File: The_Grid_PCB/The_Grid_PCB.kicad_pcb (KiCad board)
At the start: 2 copper layers, 120 x 75 mm, 104 parts, among them J1 TC2050, J10 Screw_Terminal_01x02, J11 Screw_Terminal_01x02, J12 Screw_Terminal_01x02, J13 Screw_Terminal_01x02, J14 Screw_Terminal_01x02, J15 Screw_Terminal_01x02, J16 Screw_Terminal_01x02, J17 Screw_Terminal_01x02, J2 Screw_Terminal_01x02, J3 Conn_01x02, J4 Conn_01x02, J5 Screw_Terminal_01x02, J6 Screw_Terminal_01x02, J7 Screw_Terminal_01x02, J8 Screw_Terminal_01x02, J9 Screw_Terminal_01x02, Q1 AO3400A, Q10 AO3400A, Q11 AO3400A, Q12 AO3400A, Q2 AO3400A, Q3 AO3400A, Q4 AO3400A, Q5 AO3400A, Q6 AO3400A, Q7 AO3400A, Q8 AO3400A, Q9 AO3400A, U1 STM32F030C8Tx, U2 SN65HVD11HD, U3 TPS54331DR, X1 X322516MLB4SI

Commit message: update wiring diagram again sob
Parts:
- removed the R11 at (147.0, 90.9)
- removed the R14 at (141.3, 90.1)
- removed the R8 at (179.0, 106.1)
- added C21: 47uF, PCM_JLCPCB:C_1206, F.Cu at (256.9, 87.5)
- added C22: 22uF, PCM_JLCPCB:C_0603, F.Cu at (256.0, 95.9)
- added C24: 100nF, PCM_JLCPCB:C_0805, F.Cu at (242.7, 95.5)
- added D2: LED, PCM_JLCPCB:D_0603, F.Cu at (247.0, 95.3)
- added R12: 68kΩ, PCM_JLCPCB:R_0603, F.Cu at (134.4, 92.5)
- added R16: 560Ω, PCM_JLCPCB:R_0603, F.Cu at (128.8, 93.3)
- added R17: 1.2kΩ, PCM_JLCPCB:R_0603, F.Cu at (127.0, 95.0)
- added R2: 1.5kΩ, PCM_JLCPCB:R_0603, F.Cu at (252.3, 86.9)
- added R7: 10Ω, PCM_JLCPCB:R_0603, F.Cu at (252.3, 91.4)
- added R9: 120, Resistor_THT:R_Axial_DIN0207_L6.3mm_D2.5mm_P10.16mm_Horizontal, F.Cu at (242.9, 122.0)
- added U4: AMS1117-3.3, Package_TO_SOT_SMD:SOT-223-3_TabPin2, F.Cu at (227.5, 80.8)
- C19: value 100uF -> 10uF; footprint PCM_JLCPCB:C_1206 -> PCM_JLCPCB:C_0603
- C20: value 100uF -> 47uF
- J1: footprint Connector:Tag-Connect_TC2070-IDC-FP_2x07_P1.27mm_Vertical -> Connector:Tag-Connect_TC2050-IDC-FP_2x05_P1.27mm_Vertical
- L1: value 6.8uH -> 8.2uH; footprint Inductor_SMD:L_Sumida_CDMC6D28_7.25x6.5mm -> Inductor_SMD:L_Bourns_SRP7028A_7.3x6.6mm
- R15: value 240Ω -> 200Ω
- U2: value SN65HVD11HD -> SN65HVD485EDR
- moved C20 107.8 mm to (256.9, 90.8), turned to 0 degrees
- moved C19 104.1 mm to (256.0, 93.6), turned to 0 degrees
- moved D1 62.2 mm to (222.6, 97.3)
- moved R1 62.2 mm to (222.5, 95.3)
- moved R15 14.4 mm to (127.0, 91.6)
- moved C11 12.6 mm to (157.1, 95.2)
- moved C12 12.6 mm to (163.1, 93.7)
- moved C13 12.6 mm to (154.6, 95.2)
- moved C14 12.6 mm to (149.6, 95.2)
- moved C15 12.6 mm to (149.1, 90.2)
- moved C16 12.6 mm to (140.1, 97.7)
- moved C17 12.6 mm to (131.6, 93.2)
- moved C18 12.6 mm to (137.1, 93.2)
- moved C23 12.6 mm to (134.1, 107.4)
- moved C25 12.6 mm to (134.1, 105.1)
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- renumbered C21 to C23, C22 to C25, D2 to D3, D3 to D4, R9 to R10, R10 to R11, R12 to R13, R13 to R14, R16 to R18, R17 to R19, R18 to R20, R19 to R21, R20 to R22, R21 to R23, R22 to R24, R23 to R25, R24 to R26, R25 to R27, R26 to R28, R27 to R29, R2 to R3, R28 to R30, R29 to R31, R30 to R32, R31 to R33, R32 to R34, R33 to R35, R34 to R36, R35 to R37, R36 to R38, R37 to R39, R3 to R4, R38 to R40, R39 to R41, R40 to R42, R41 to R43, R4 to R5, R5 to R6, R7 to R8
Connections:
- C10 pad 1: +3.3V -> +5V
- C19 pad 1: +3.3V -> +5V
- C20 pad 1: +3.3V -> GND
- C20 pad 2: GND -> +5V
- C23 pad 1: +3.3V -> +5V
- C25 pad 1: +3.3V -> +5V
- L1 pad 2: +3.3V -> +5V
- R13 pad 1: +3.3V -> +5V
- R15 pad 1: Net-(R14-Pad2) -> Net-(U3-VSENSE)
- R15 pad 2: GND -> Net-(R15-Pad2)
- R5 pad 1: +3.3V -> +5V
- U2 pad 8: +3.3V -> +5V
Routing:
- net GND: track 574.4 -> 457.6 mm
- net +3.3V: track 280.9 -> 192.2 mm, vias 7 -> 6
- net /R4: track 55.0 -> 0.00 mm
- net /G4: track 52.8 -> 0.00 mm
- net /B3: track 46.2 -> 0.00 mm
- net /G3: track 44.6 -> 0.00 mm
- net /B4: track 44.1 -> 0.00 mm
- net /R3: track 43.0 -> 0.00 mm
- net +5V: track 0.00 -> 35.9 mm
- net /B1: track 35.7 -> 0.00 mm
- net /B2: track 33.7 -> 0.00 mm
- net /R2: track 31.4 -> 0.00 mm
- net /G2: track 31.2 -> 0.00 mm
- net /R1: track 34.6 -> 7.89 mm
- net /G1: track 33.1 -> 6.86 mm
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- added copper zone on F.Cu, net +5V
- removed copper zone on F.Cu, net +3.3V
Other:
- board size 120 x 75 mm -> 120 x 60 mm

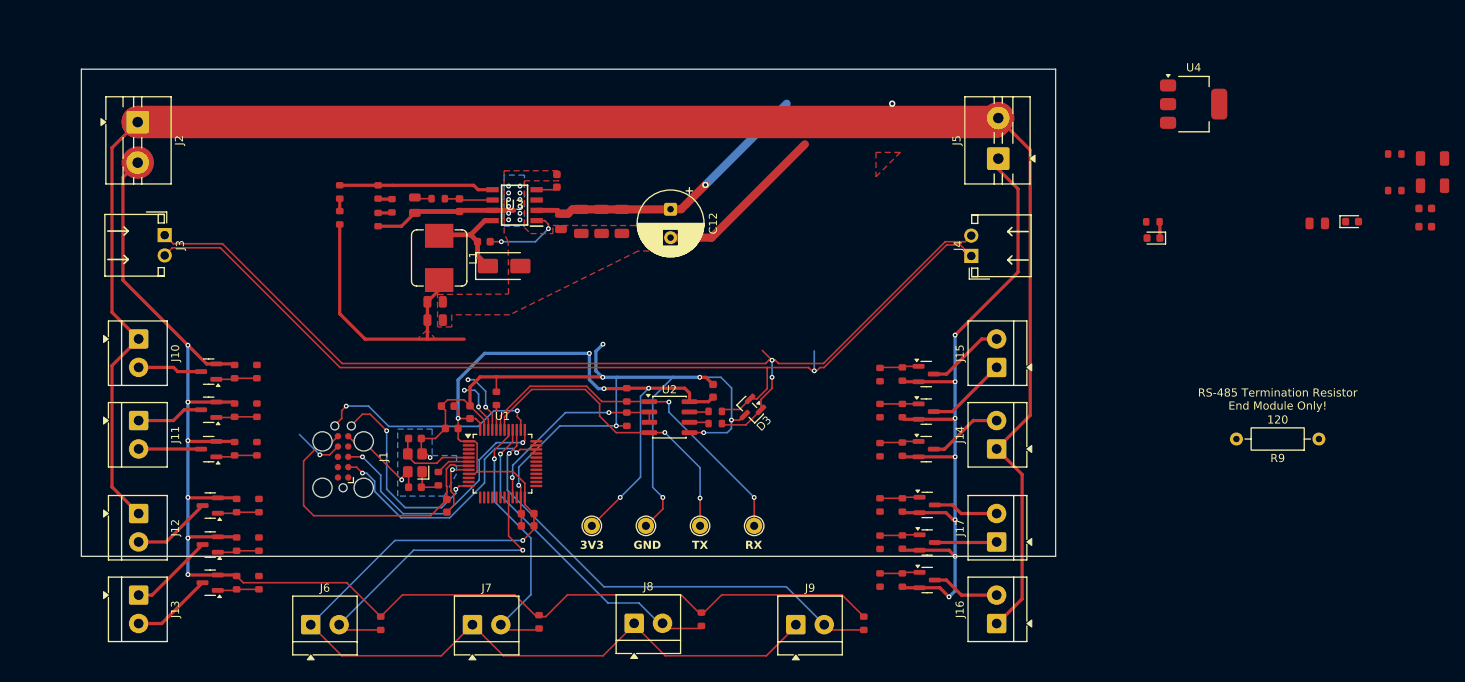
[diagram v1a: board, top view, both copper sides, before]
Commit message: revised pcb nevin/miguel feedback
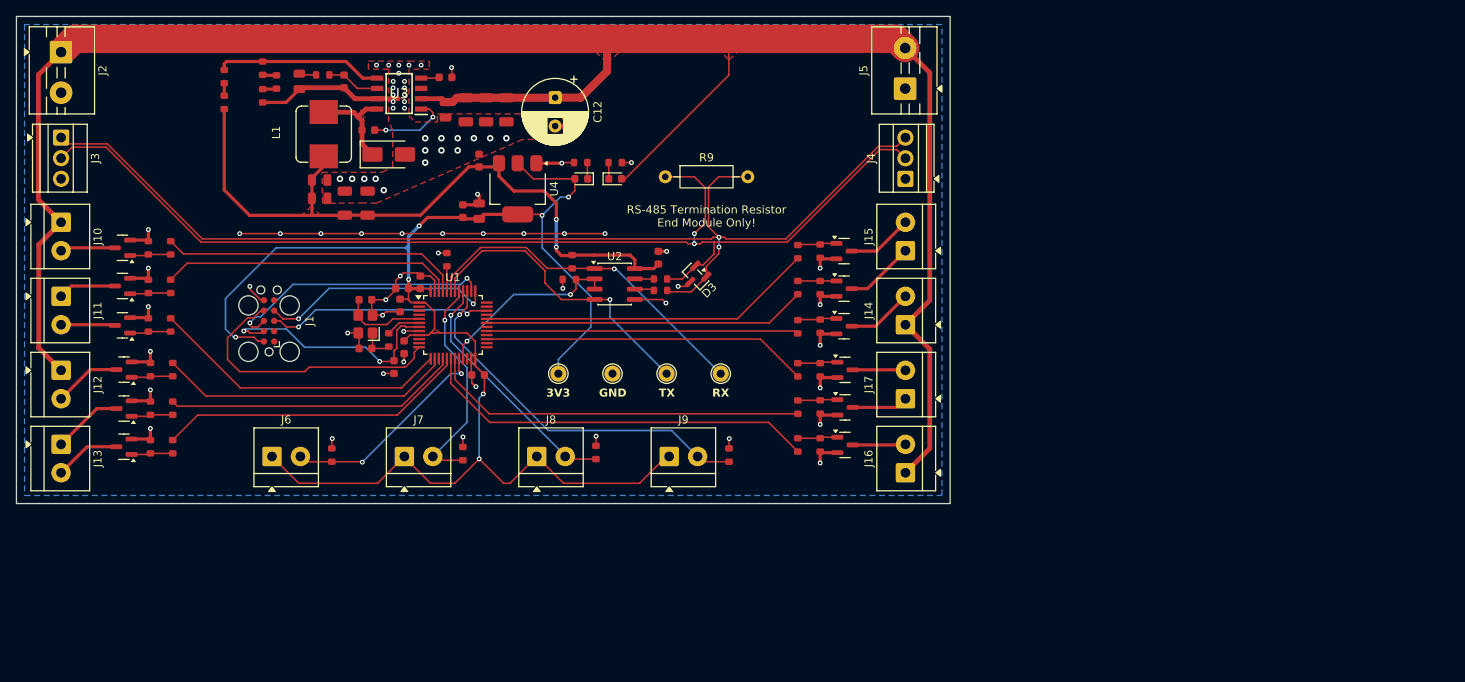
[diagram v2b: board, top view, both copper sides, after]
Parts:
- removed the R6 at (157.7, 119.6)
- removed the R6 at (168.6, 118.6)
- added R6: 10kΩ, PCM_JLCPCB:R_0603, F.Cu at (150.6, 102.4)
- J3, J4: value Conn_01x02 -> Screw_Terminal_01x03; footprint james_custom_footprint_library:JST_XH_B02B-XH-A_02x2.50mm_7.32x7.5_RightAngle -> TerminalBlock:TerminalBlock_Xinya_XY308-2.54-3P_1x03_P2.54mm_Horizontal
- moved C20 134.0 mm to (123.0, 93.0), turned to -90 degrees
- moved C21 131.3 mm to (125.8, 93.0), turned to -90 degrees
- moved C22 118.6 mm to (137.5, 94.0), turned to 90 degrees
- moved C19 116.7 mm to (139.5, 87.8), turned to 90 degrees
- moved C24 103.3 mm to (139.5, 94.0), turned to 90 degrees
- moved R2 96.0 mm to (156.2, 88.0)
- moved R7 91.1 mm to (161.8, 102.3)
- moved D2 90.9 mm to (156.2, 90.0)
- moved R9 86.7 mm to (162.4, 89.8), turned to 0 degrees
- moved U4 83.9 mm to (144.2, 91.2), turned to -90 degrees
- moved D1 70.9 mm to (152.1, 90.0)
- moved R1 70.9 mm to (152.0, 88.0)
- moved C5 32.8 mm to (132.2, 102.8), turned to 90 degrees
- moved R19 26.5 mm to (170.3, 124.0)
- moved J9 25.9 mm to (162.9, 124.2)
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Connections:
- J4 pad 1: /RSB -> GND
- J4 pad 2: /RSA -> /RSB
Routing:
- net GND: track 457.6 -> 162.3 mm, vias 36 -> 75
- net +5V: track 35.9 -> 86.0 mm, vias 0 -> 2
- net /R4: track 0.00 -> 49.3 mm
- net /G4: track 0.00 -> 46.5 mm
- net /B3: track 0.00 -> 41.4 mm
- net /B4: track 0.00 -> 40.2 mm
- net /G3: track 0.00 -> 39.8 mm
- net /R3: track 0.00 -> 38.4 mm
- net /B2: track 0.00 -> 38.4 mm
- net /B1: track 0.00 -> 37.1 mm
- net /G2: track 0.00 -> 36.4 mm
- net /R2: track 0.00 -> 36.3 mm
- net /R1: track 7.89 -> 37.2 mm, vias 2 -> 0
- net /G1: track 6.86 -> 36.1 mm, vias 2 -> 0
- net /Microswitch4: track 58.9 -> 46.4 mm
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- added copper zone on F.Cu, net +24V
- added copper zone on B.Cu, net +3.3V
- added copper zone on F.Cu, net +3.3V
- added copper zone on F.Cu, net Net-(U3-PH)
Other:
- board size 120 x 60 mm -> 115 x 60 mm

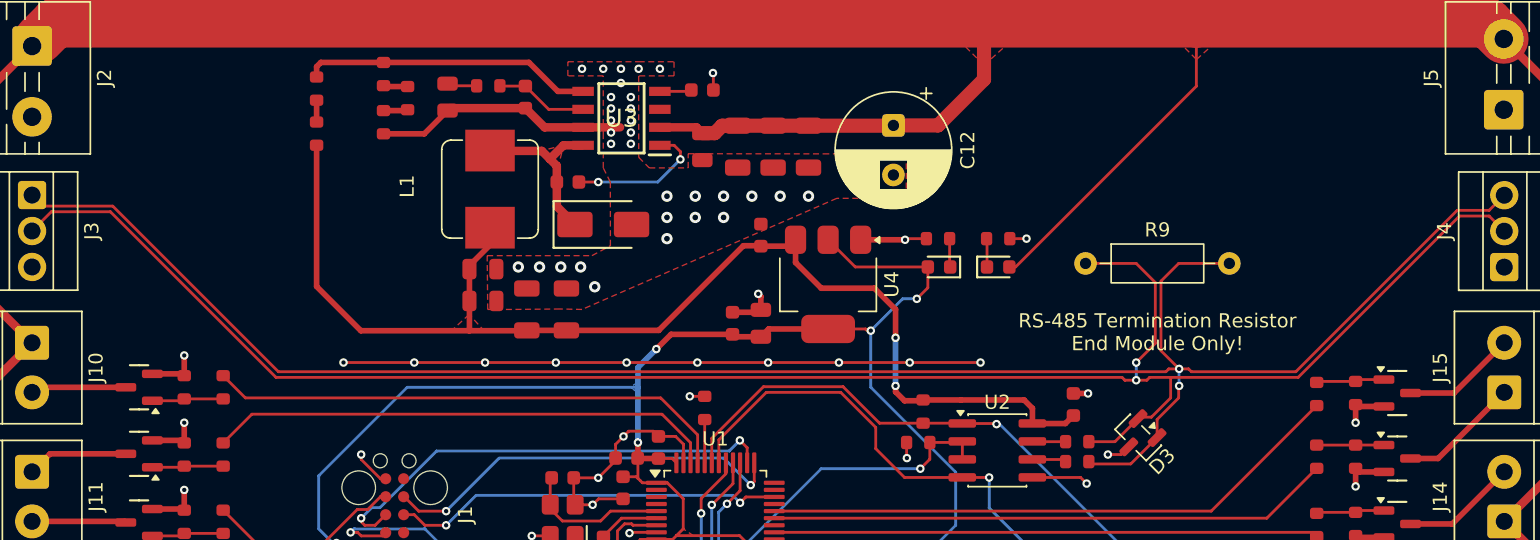
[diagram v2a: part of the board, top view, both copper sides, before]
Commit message: add silkscreen, move termination res
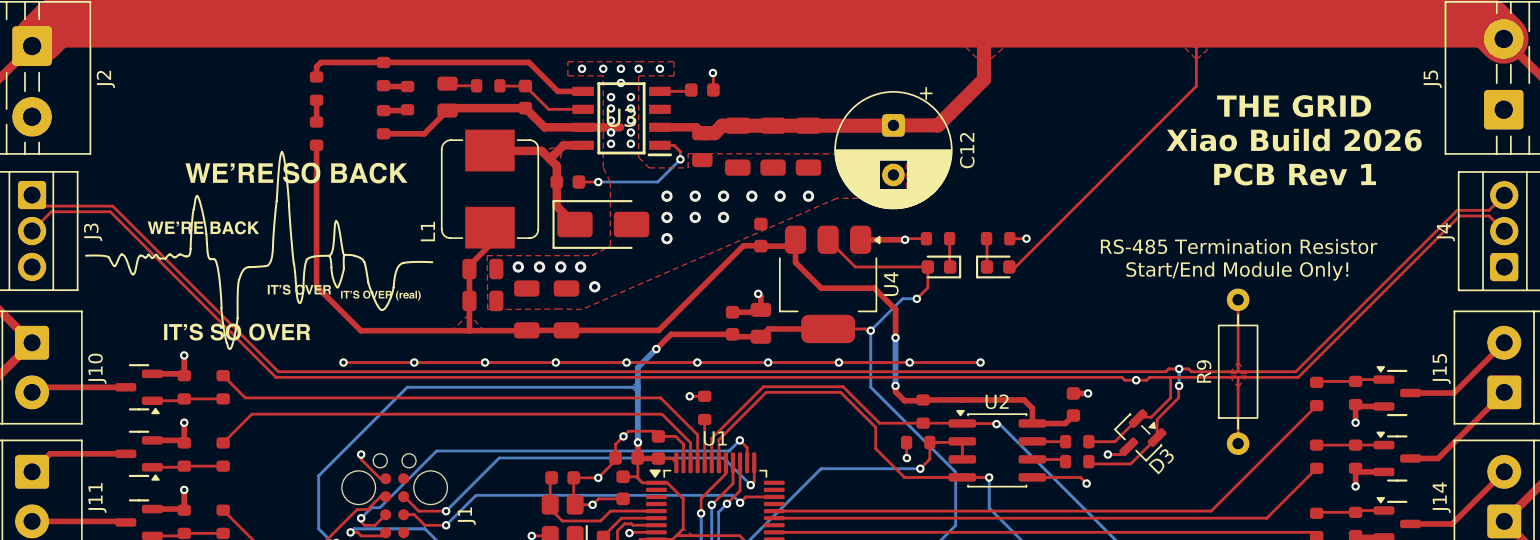
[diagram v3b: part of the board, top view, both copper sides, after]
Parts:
- moved R9 16.7 mm to (173.2, 102.5), turned to 90 degrees
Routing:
- net /RSB: track 136.2 -> 127.9 mm, vias 2 -> 1
- net /RSA: track 137.5 -> 130.5 mm
- added copper zone on F.Cu, net /RSA
- added copper zone on F.Cu, net /RSB
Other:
- board text added: "RS-485 Termination Resistor Start/End Module Only!"
- board text added: "THE GRID Xiao Build 2026 PCB Rev 1"
- board text removed: "RS-485 Termination Resistor End Module Only!"
